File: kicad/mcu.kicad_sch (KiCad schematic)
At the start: 3 parts

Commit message: Remove some horizontal connectors and replace with vertical
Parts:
- R401, R402: JLC Qty 10200 -> 10155
- R403: JLC Qty 9700 -> 9610
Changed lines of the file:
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@@
 			)
 		)
-		(property "JLC Qty" "10200"
+		(property "JLC Qty" "10155"
 			(at 38.1 138.43 0)
 			(hide yes)
@@
 			)
 		)
-		(property "JLC Qty" "9700"
+		(property "JLC Qty" "9610"
 			(at 208.28 54.61 0)
 			(hide yes)
@@
 			)
 		)
-		(property "JLC Qty" "10200"
+		(property "JLC Qty" "10155"
 			(at 38.1 120.65 0)
 			(hide yes)
@@
 		)
 		(property "Value" "PWR_FLAG"
-			(at 81.28 22.86 0)
-			(show_name no)
-			(do_not_autoplace no)
-			(effects
-				(font
-					(size 1.27 1.27)
-				)
-			)
-		)
+			(at 83.82 26.6699 0)
+			(show_name no)
+			(do_not_autoplace no)
+			(effects
+				(font
+					(size 1.27 1.27)
+				)
+				(justify left)
+			)
+		)

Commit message: Update date
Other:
- title: mouse-joystick-pcb -> Orb Weaver Design Block Mining
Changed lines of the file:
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@@
 	(paper "A4")
 	(title_block
-		(title "mouse-joystick-pcb")
-		(date "2026-08-25")
+		(title "Orb Weaver Design Block Mining")
+		(date "2026-08-26")
 		(rev "0.3")
 		(company "Janelia Research Campus")

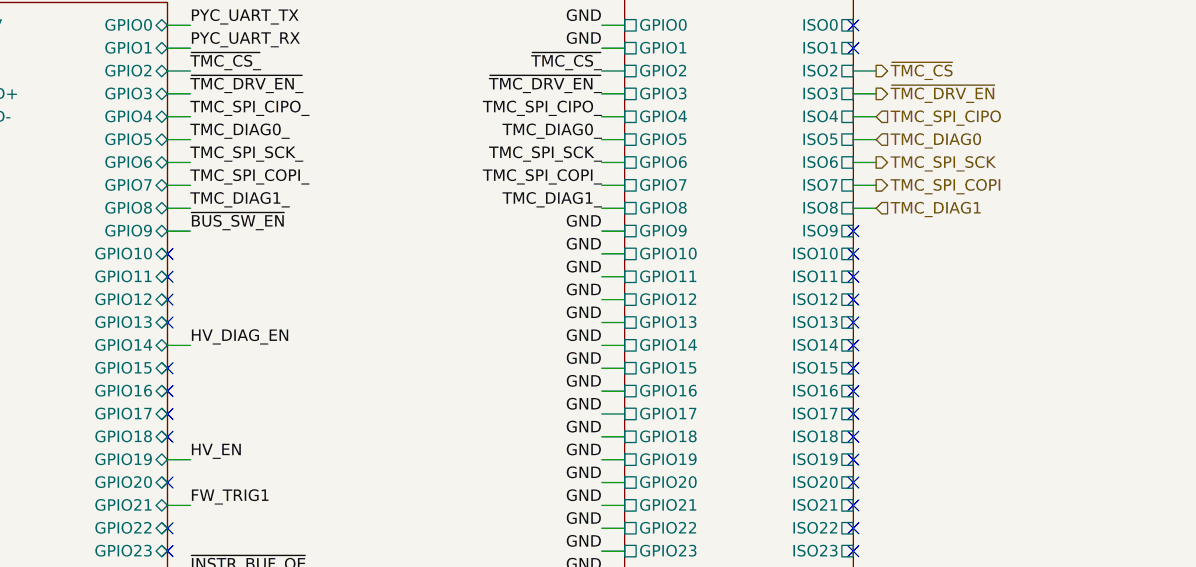
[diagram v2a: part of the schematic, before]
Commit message: Add DAC design block for angle output
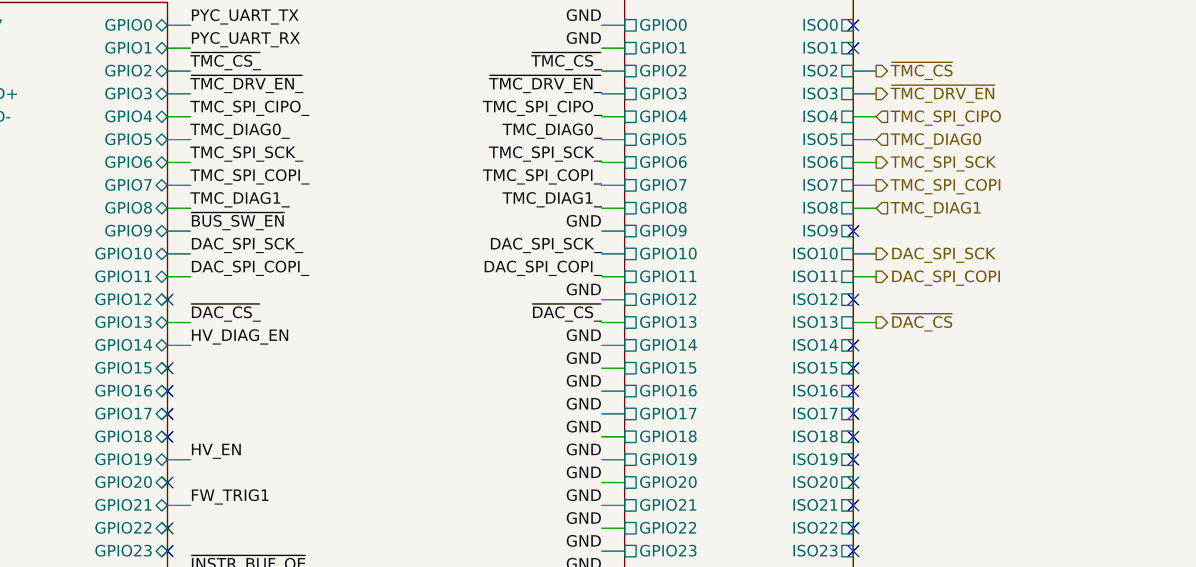
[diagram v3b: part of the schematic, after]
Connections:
- no-connect marks 35 -> 29
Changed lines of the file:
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@@
-	)
-	(no_connect
-		(at 101.6 104.14)
 	)
 	(no_connect
@@
 	)
 	(no_connect
-		(at 101.6 111.76)
-	)
-	(no_connect
 		(at 177.8 139.7)
 	)
@@
 	)
 	(no_connect
-		(at 177.8 111.76)
-	)
-	(no_connect
 		(at 101.6 121.92)
 	)
@@
 	)
 	(no_connect
-		(at 101.6 106.68)
-	)
-	(no_connect
 		(at 177.8 142.24)
 	)
@@
 	)
 	(no_connect
-		(at 177.8 106.68)
-	)
-	(no_connect
 		(at 177.8 132.08)
 	)
@@
 	)
 	(no_connect
-		(at 177.8 104.14)
-	)
-	(no_connect
 		(at 177.8 119.38)
 	)
@@
 	(wire
 		(pts
+			(xy 177.8 111.76) (xy 180.34 111.76)
+		)
+		(stroke
+			(width 0)
+			(type default)
+		)
+	)
+	(wire
+		(pts
 			(xy 38.1 114.3) (xy 38.1 111.76)
 		)
@@
 	(wire
 		(pts
+			(xy 177.8 106.68) (xy 180.34 106.68)
+		)
+		(stroke
+			(width 0)
+			(type default)
+		)
+	)
+	(wire
+		(pts
 			(xy 152.4 91.44) (xy 149.86 91.44)
 		)
@@
 	(wire
 		(pts
+			(xy 177.8 104.14) (xy 180.34 104.14)
+		)
+		(stroke
+			(width 0)
+			(type default)
+		)
+	)
+	(wire
+		(pts
 			(xy 50.8 35.56) (xy 53.34 35.56)
 		)
@@
 	(wire
 		(pts
+			(xy 101.6 106.68) (xy 104.14 106.68)
+		)
+		(stroke
+			(width 0)
+			(type default)
+		)
+	)
+	(wire
+		(pts
 			(xy 152.4 93.98) (xy 149.86 93.98)
 		)
@@
 	(wire
 		(pts
+			(xy 101.6 104.14) (xy 104.14 104.14)
+		)
+		(stroke
+			(width 0)
+			(type default)
+		)
+	)
+	(wire
+		(pts
 			(xy 38.1 129.54) (xy 40.64 129.54)
 		)
@@
 		(pts
 			(xy 101.6 86.36) (xy 104.14 86.36)
+		)
+		(stroke
+			(width 0)
+			(type default)
+		)
+	)
+	(wire
+		(pts
+			(xy 101.6 111.76) (xy 104.14 111.76)
 		)
 		(stroke
@@
 		)
 	)
-	(label "GND"
-		(at 149.86 104.14 180)
-		(effects
-			(font
-				(size 1.27 1.27)
-			)
-			(justify right bottom)
-		)
-	)
 	(label "FW_TRIG0"
 		(at 104.14 142.24 0)
@@
 		)
 	)
+	(label "~{DAC_CS_}"
+		(at 104.14 111.76 0)
+		(effects
+			(font
+				(size 1.27 1.27)
+			)
+			(justify left bottom)
+		)
+	)
 	(label "PYC_UART_TX"
 		(at 53.34 35.56 0)
@@
 		)
 	)
+	(label "DAC_SPI_SCK_"
+		(at 104.14 104.14 0)
+		(effects
+			(font
+				(size 1.27 1.27)
+			)
+			(justify left bottom)
+		)
+	)
 	(label "GND"
 		(at 149.86 137.16 180)
@@
 		)
 	)
+	(label "DAC_SPI_COPI_"
+		(at 149.86 106.68 180)
+		(effects
+			(font
+				(size 1.27 1.27)
+			)
+			(justify right bottom)
+		)
+	)
 	(label "~{HV_FAULT}"
 		(at 53.34 55.88 0)
@@
 		)
 	)
+	(label "~{DAC_CS_}"
+		(at 149.86 111.76 180)
+		(effects
+			(font
+				(size 1.27 1.27)
+			)
+			(justify right bottom)
+		)
+	)
 	(label "+3.3V_MCU"
 		(at 208.28 48.26 90)
@@
 		)
 	)
+	(label "DAC_SPI_SCK_"
+		(at 149.86 104.14 180)
+		(effects
+			(font
+				(size 1.27 1.27)
+			)
+			(justify right bottom)
+		)
+	)
 	(label "GND"
 		(at 149.86 129.54 180)
-		(effects
-			(font
-				(size 1.27 1.27)
-			)
-			(justify right bottom)
-		)
-	)
-	(label "GND"
-		(at 149.86 111.76 180)
-		(effects
-			(font
-				(size 1.27 1.27)
-			)
-			(justify right bottom)
-		)
-	)
-	(label "GND"
-		(at 149.86 106.68 180)
 		(effects
 			(font
@@
 	(label "SW_RAIL_SENSE"
 		(at 38.1 111.76 90)
+		(effects
+			(font
+				(size 1.27 1.27)
+			)
+			(justify left bottom)
+		)
+	)
+	(label "DAC_SPI_COPI_"
+		(at 104.14 106.68 0)
 		(effects
 			(font
@@
 		)
 	)
+	(hierarchical_label "~{DAC_CS}"
+		(shape output)
+		(at 180.34 111.76 0)
+		(effects
+			(font
+				(size 1.27 1.27)
+			)
+			(justify left)
+		)
+	)
+	(hierarchical_label "DAC_SPI_SCK"
+		(shape output)
+		(at 180.34 104.14 0)
+		(effects
+			(font
+				(size 1.27 1.27)
+			)
+			(justify left)
+		)
+	)
 	(hierarchical_label "GND"
 		(shape passive)
@@
 		)
 	)
+	(hierarchical_label "DAC_SPI_COPI"
+		(shape output)
+		(at 180.34 106.68 0)
+		(effects
+			(font
+				(size 1.27 1.27)
+			)
+			(justify left)
+		)
+	)

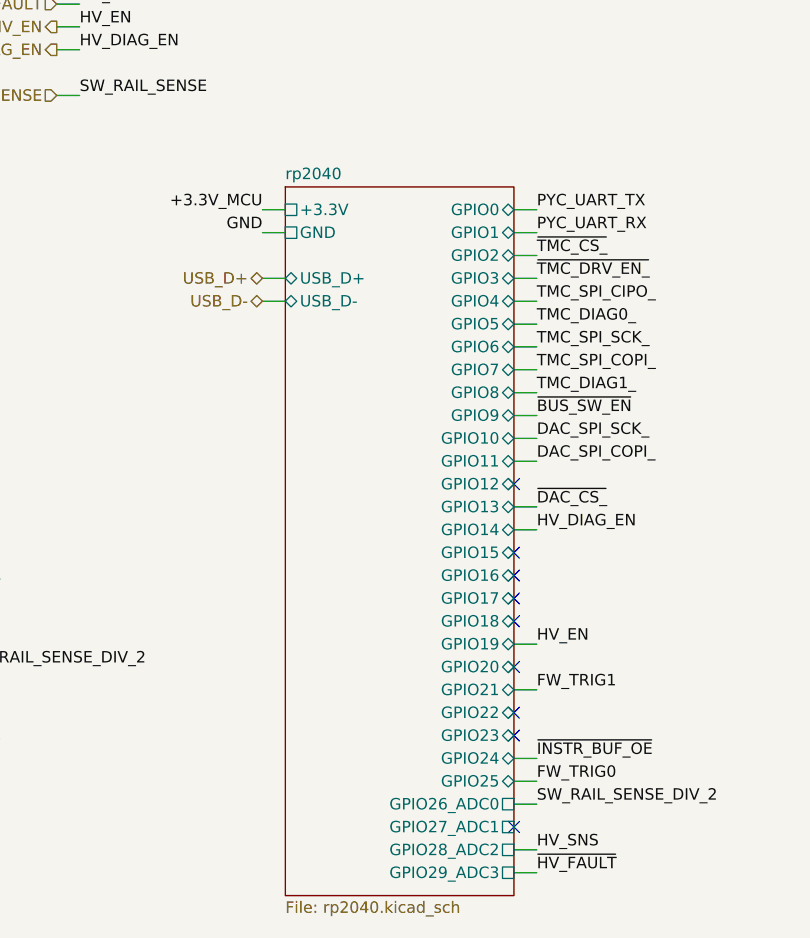
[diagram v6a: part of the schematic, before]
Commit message: Remove some design blocks for modifications
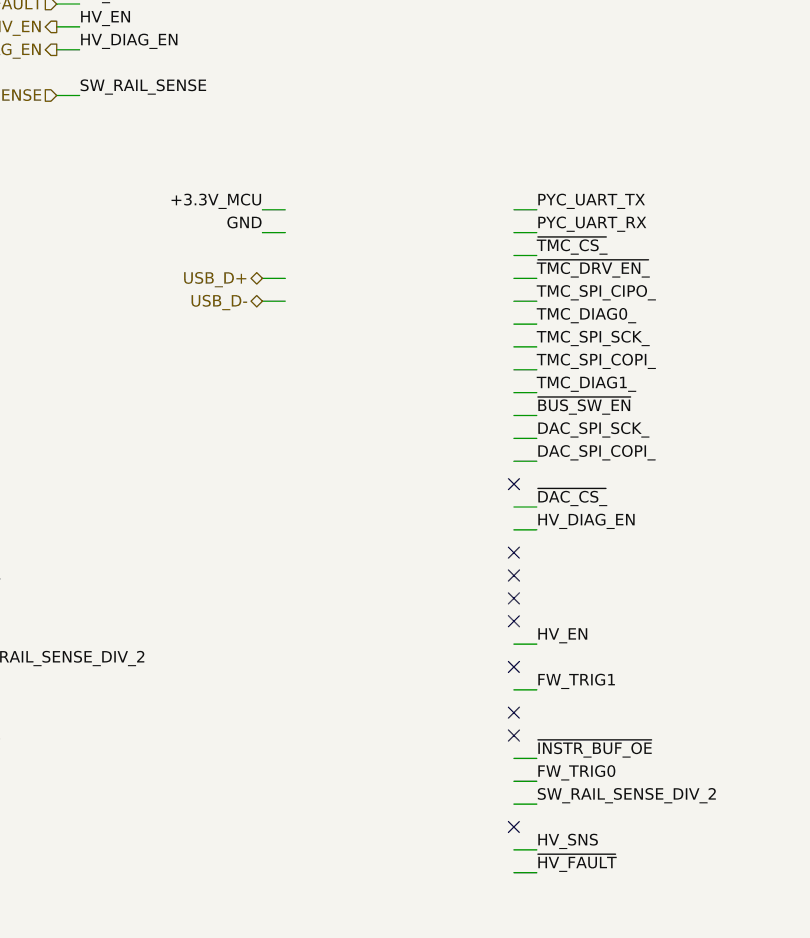
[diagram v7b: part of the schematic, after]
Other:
- removed sheet rp2040

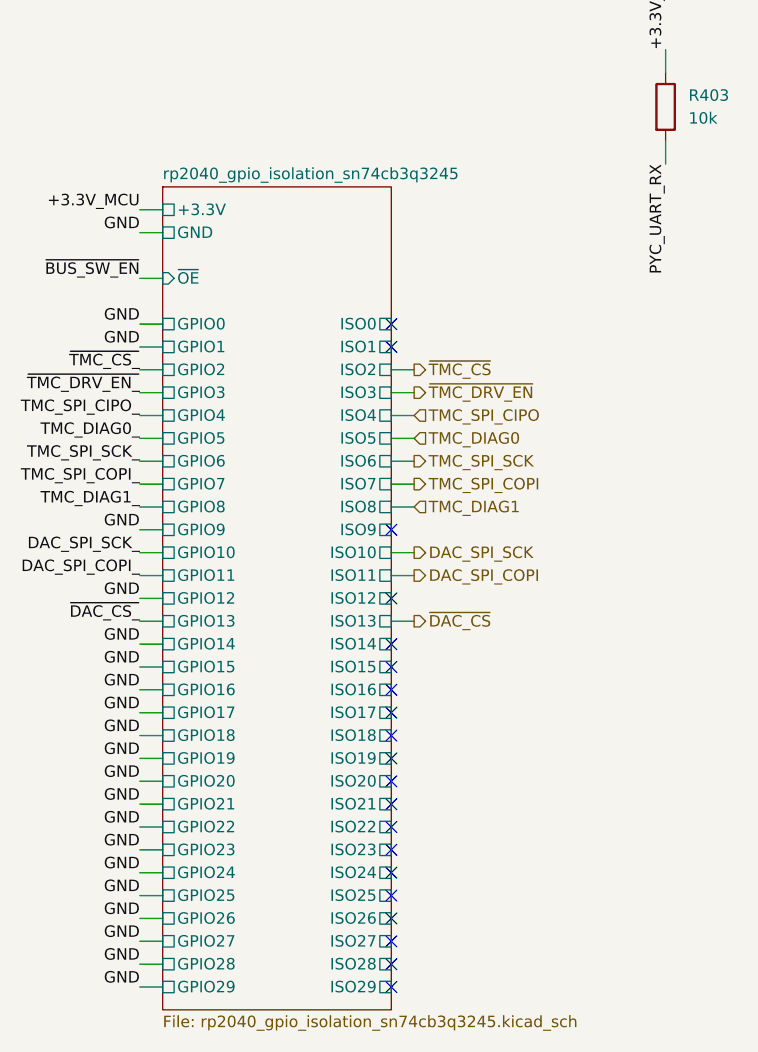
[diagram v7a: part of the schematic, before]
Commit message: Update docs with mouse-joystick-pcb v1.0 pinout
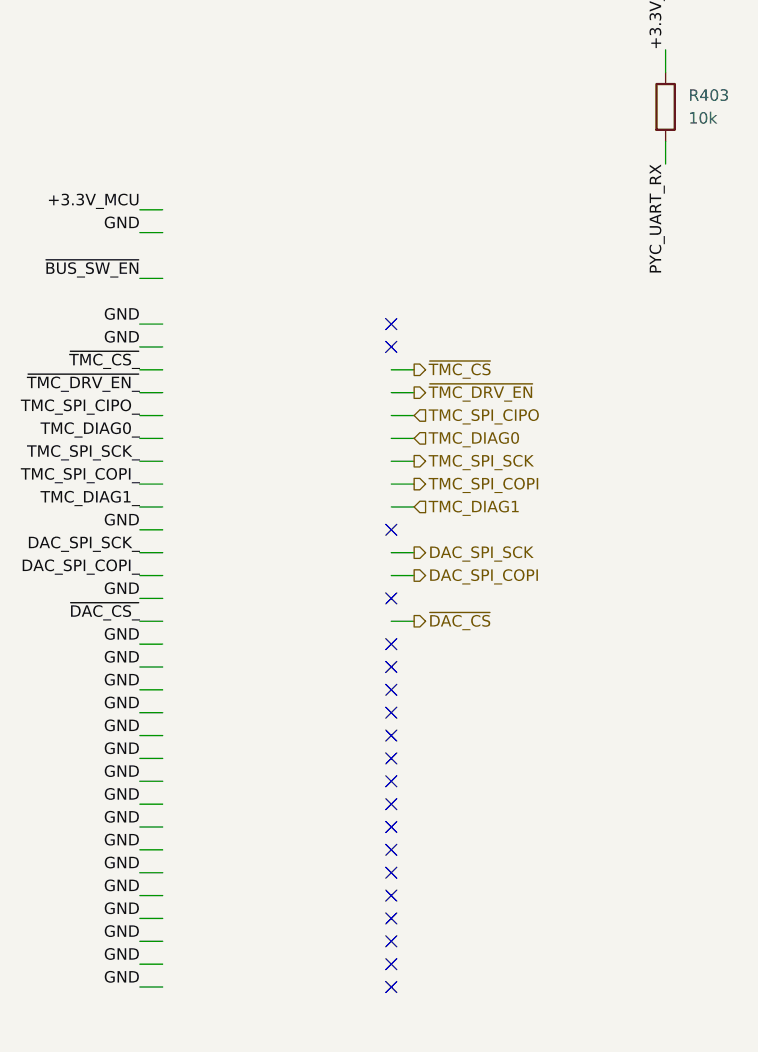
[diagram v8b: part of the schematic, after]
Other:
- removed sheet rp2040_gpio_isolation_sn74cb3q3245
- title: Orb Weaver Design Block Mining -> mouse-joystick-pcb
